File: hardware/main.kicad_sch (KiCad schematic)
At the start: 26 parts, among them J2 Micro_SD_Card, SW1 SW_DIP_x01, SW2 SW_DIP_x01, SW3 SW_DIP_x01, SW4 SW_DIP_x01, SW5 SW_DIP_x01, SW6 SW_DIP_x01, SW7 SW_DIP_x01, U1 SN74LVC245APW, U2 SN74LVC245APW, U3 SN74LVC245APW, U4 Z084000xP

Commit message: update pcb files
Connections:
- net KEYB: now also A1.34 (GPIO28_ADC2); no longer A1.32 (GPIO27_ADC1)
- net IORQ: now reaches U4.20 (~{IORQ})
- net IORQ: now also A1.31 (GPIO26_ADC0)
- net WR: now reaches U4.22 (~{WR})
- net WR: now also A1.32 (GPIO27_ADC1)
- no-connect marks 11 -> 7
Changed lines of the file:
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@@
 		(title "Z80neo")
 		(date "25/10/25")
-		(rev "0.1")
+		(rev "0.2")
 		(company "Jauria Studios")
 	)
@@
 	)
 	(no_connect
-		(at 260.35 127)
-	)
-	(no_connect
-		(at 27.94 81.28)
-	)
-	(no_connect
 		(at 27.94 68.58)
 	)
@@
 	)
 	(no_connect
-		(at 260.35 132.08)
-	)
-	(no_connect
-		(at 27.94 76.2)
-	)
-	(no_connect
 		(at 100.33 165.1)
 	)
@@
 		)
 	)
+	(wire
+		(pts
+			(xy 260.35 129.54) (xy 266.7 129.54)
+		)
+		(stroke
+			(width 0)
+			(type default)
+		)
+	)
 	(bus
 		(pts
@@
 	(wire
 		(pts
-			(xy 260.35 129.54) (xy 266.7 129.54)
+			(xy 260.35 132.08) (xy 266.7 132.08)
 		)
 		(stroke
@@
 	(bus
 		(pts
-			(xy 68.58 99.06) (xy 68.58 101.6)
+			(xy 68.58 100.33) (xy 68.58 101.6)
 		)
 		(stroke
@@
 		)
 	)
+	(wire
+		(pts
+			(xy 27.94 81.28) (xy 21.59 81.28)
+		)
+		(stroke
+			(width 0)
+			(type default)
+		)
+	)
 	(bus
 		(pts
@@
 	(wire
 		(pts
+			(xy 260.35 127) (xy 266.7 127)
+		)
+		(stroke
+			(width 0)
+			(type default)
+		)
+	)
+	(wire
+		(pts
 			(xy 210.82 121.92) (xy 214.63 121.92)
 		)
@@
 	(bus
 		(pts
-			(xy 68.58 99.06) (xy 96.52 99.06)
+			(xy 68.58 100.33) (xy 96.52 100.33)
 		)
 		(stroke
@@
 	(bus
 		(pts
-			(xy 96.52 99.06) (xy 96.52 104.14)
+			(xy 96.52 100.33) (xy 96.52 104.14)
 		)
 		(stroke
@@
 	(wire
 		(pts
+			(xy 27.94 76.2) (xy 21.59 76.2)
+		)
+		(stroke
+			(width 0)
+			(type default)
+		)
+	)
+	(wire
+		(pts
 			(xy 53.34 91.44) (xy 63.5 91.44)
 		)
@@
 		)
 	)
+	(label "B[0..7]"
+		(at 162.56 19.05 0)
+		(effects
+			(font
+				(size 1.27 1.27)
+			)
+			(justify left bottom)
+		)
+	)
 	(label "D0"
 		(at 105.41 106.68 180)
@@
 		)
 	)
+	(label "D[0..7]"
+		(at 74.93 100.33 0)
+		(effects
+			(font
+				(size 1.27 1.27)
+			)
+			(justify left bottom)
+		)
+	)
 	(label "B2"
 		(at 175.26 54.61 0)
@@
 		)
 	)
+	(label "A[0..15]"
+		(at 77.47 22.86 0)
+		(effects
+			(font
+				(size 1.27 1.27)
+			)
+			(justify left bottom)
+		)
+	)
 	(label "D3"
 		(at 105.41 114.3 180)
@@
 		)
 	)
+	(global_label "IORQ"
+		(shape input)
+		(at 21.59 76.2 180)
+		(fields_autoplaced yes)
+		(effects
+			(font
+				(size 1.27 1.27)
+			)
+			(justify right)
+		)
+		(property "Intersheetrefs" "${INTERSHEET_REFS}"
+			(at 14.069 76.2 0)
+			(effects
+				(font
+					(size 1.27 1.27)
+				)
+				(justify right)
+				(hide yes)
+			)
+		)
+	)
 	(global_label "SDA"
 		(shape input)
@@
 		)
 	)
+	(global_label "WR"
+		(shape input)
+		(at 21.59 81.28 180)
+		(fields_autoplaced yes)
+		(effects
+			(font
+				(size 1.27 1.27)
+			)
+			(justify right)
+		)
+		(property "Intersheetrefs" "${INTERSHEET_REFS}"
+			(at 15.8834 81.28 0)
+			(effects
+				(font
+					(size 1.27 1.27)
+				)
+				(justify right)
+				(hide yes)
+			)
+		)
+	)
 	(global_label "SEL2"
 		(shape input)
@@
 		)
 	)
+	(global_label "IORQ"
+		(shape input)
+		(at 266.7 127 0)
+		(fields_autoplaced yes)
+		(effects
+			(font
+				(size 1.27 1.27)
+			)
+			(justify left)
+		)
+		(property "Intersheetrefs" "${INTERSHEET_REFS}"
+			(at 274.221 127 0)
+			(effects
+				(font
+					(size 1.27 1.27)
+				)
+				(justify left)
+				(hide yes)
+			)
+		)
+	)
 	(global_label "RD"
 		(shape input)
@@
 		)
 	)
+	(global_label "WR"
+		(shape input)
+		(at 266.7 129.54 0)
+		(fields_autoplaced yes)
+		(effects
+			(font
+				(size 1.27 1.27)
+			)
+			(justify left)
+		)
+		(property "Intersheetrefs" "${INTERSHEET_REFS}"
+			(at 272.4066 129.54 0)
+			(effects
+				(font
+					(size 1.27 1.27)
+				)
+				(justify left)
+				(hide yes)
+			)
+		)
+	)
 	(global_label "MOSI"
 		(shape input)
@@
 	(global_label "KEYB"
 		(shape input)
-		(at 266.7 129.54 0)
+		(at 266.7 132.08 0)
 		(fields_autoplaced yes)
 		(effects
@@
 		)
 		(property "Intersheetrefs" "${INTERSHEET_REFS}"
-			(at 274.4628 129.54 0)
+			(at 274.4628 132.08 0)
 			(effects
 				(font

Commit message: pcb routing
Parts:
- added R10: R_Small, symbol Device:R_Small
- C1, C2, C3: footprint (none) -> Capacitor_SMD:C_0603_1608Metric_Pad1.08x0.95mm_HandSolder
- D1: footprint (none) -> LED_SMD:LED_0603_1608Metric_Pad1.05x0.95mm_HandSolder
- J2: footprint (none) -> Connector_PinSocket_2.54mm:PinSocket_1x08_P2.54mm_Horizontal
- R1, R2, R3, R4, R5, R6, R7, R8, R9: footprint (none) -> Resistor_SMD:R_0603_1608Metric_Pad0.98x0.95mm_HandSolder
- SW1, SW2, SW3, SW4, SW5, SW6, SW7: footprint (none) -> Button_Switch_THT:SW_PUSH_6mm
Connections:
- net +5V: now also R10.1; no longer D1.2 (A)
- new net: D1.2 (A), R10.2
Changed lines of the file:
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@@
 	(wire
 		(pts
+			(xy 266.7 39.37) (xy 266.7 44.45)
+		)
+		(stroke
+			(width 0)
+			(type default)
+		)
+	)
+	(wire
+		(pts
 			(xy 266.7 58.42) (xy 266.7 60.96)
 		)
@@
 			)
 		)
-		(property "Footprint" ""
+		(property "Footprint" "Resistor_SMD:R_0603_1608Metric_Pad0.98x0.95mm_HandSolder"
 			(at 106.68 97.79 0)
 			(effects
@@
 			)
 		)
-		(property "Footprint" ""
+		(property "Footprint" "Resistor_SMD:R_0603_1608Metric_Pad0.98x0.95mm_HandSolder"
 			(at 171.45 144.78 0)
 			(effects
@@
 			)
 		)
-		(property "Footprint" ""
+		(property "Footprint" "Resistor_SMD:R_0603_1608Metric_Pad0.98x0.95mm_HandSolder"
 			(at 40.64 167.64 0)
 			(effects
@@
 	(symbol
 		(lib_id "power:+5V")
-		(at 266.7 49.53 0)
+		(at 266.7 39.37 0)
 		(unit 1)
 		(exclude_from_sim no)
@@
 		(on_board yes)
 		(dnp no)
-		(fields_autoplaced yes)
 		(property "Reference" "#PWR015"
-			(at 266.7 53.34 0)
+			(at 266.7 43.18 0)
 			(effects
 				(font
@@
 		)
 		(property "Value" "+5V"
-			(at 266.7 44.45 0)
+			(at 266.7 34.29 0)
 			(effects
 				(font
@@
 		)
 		(property "Footprint" ""
-			(at 266.7 49.53 0)
+			(at 266.7 39.37 0)
 			(effects
 				(font
@@
 		)
 		(property "Datasheet" ""
-			(at 266.7 49.53 0)
+			(at 266.7 39.37 0)
 			(effects
 				(font
@@
 		)
 		(property "Description" "Power symbol creates a global label with name \"+5V\""
-			(at 266.7 49.53 0)
+			(at 266.7 39.37 0)
 			(effects
 				(font
@@
 			)
 		)
-		(property "Footprint" ""
+		(property "Footprint" "Capacitor_SMD:C_0603_1608Metric_Pad1.08x0.95mm_HandSolder"
 			(at 240.03 33.02 0)
 			(effects
@@
 			)
 		)
-		(property "Footprint" ""
+		(property "Footprint" "Resistor_SMD:R_0603_1608Metric_Pad0.98x0.95mm_HandSolder"
 			(at 171.45 152.4 0)
 			(effects
@@
 			)
 		)
-		(property "Footprint" ""
+		(property "Footprint" "Button_Switch_THT:SW_PUSH_6mm"
 			(at 162.56 148.59 0)
 			(effects
@@
 			)
 		)
-		(property "Footprint" ""
+		(property "Footprint" "Resistor_SMD:R_0603_1608Metric_Pad0.98x0.95mm_HandSolder"
 			(at 146.05 40.64 0)
 			(effects
@@
 	)
 	(symbol
+		(lib_id "Device:R_Small")
+		(at 266.7 46.99 0)
+		(unit 1)
+		(exclude_from_sim no)
+		(in_bom yes)
+		(on_board yes)
+		(dnp no)
+		(property "Reference" "R10"
+			(at 260.604 47.244 0)
+			(effects
+				(font
+					(size 1.016 1.016)
+				)
+				(justify left)
+			)
+		)
+		(property "Value" "R_Small"
+			(at 269.24 48.2599 0)
+			(effects
+				(font
+					(size 1.27 1.27)
+				)
+				(justify left)
+			)
+		)
+		(property "Footprint" ""
+			(at 266.7 46.99 0)
+			(effects
+				(font
+					(size 1.27 1.27)
+				)
+				(hide yes)
+			)
+		)
+		(property "Datasheet" "~"
+			(at 266.7 46.99 0)
+			(effects
+				(font
+					(size 1.27 1.27)
+				)
+				(hide yes)
+			)
+		)
+		(property "Description" "Resistor, small symbol"
+			(at 266.7 46.99 0)
+			(effects
+				(font
+					(size 1.27 1.27)
+				)
+				(hide yes)
+			)
+		)
+		(pin "2"
+		)
+		(pin "1"
+		)
+		(instances
+			(project ""
+				(path "/7ca8aba6-072c-4d14-9481-2a37d5b8002f"
+					(reference "R10")
+					(unit 1)
+				)
+			)
+		)
+	)
+	(symbol
 		(lib_id "power:+3.3V")
 		(at 278.13 109.22 0)
@@
 			)
 		)
-		(property "Footprint" ""
+		(property "Footprint" "Resistor_SMD:R_0603_1608Metric_Pad0.98x0.95mm_HandSolder"
 			(at 171.45 137.16 0)
 			(effects
@@
 			)
 		)
-		(property "Footprint" ""
+		(property "Footprint" "Button_Switch_THT:SW_PUSH_6mm"
 			(at 162.56 140.97 0)
 			(effects
@@
 			)
 		)
-		(property "Footprint" ""
+		(property "Footprint" "Resistor_SMD:R_0603_1608Metric_Pad0.98x0.95mm_HandSolder"
 			(at 171.45 160.02 0)
 			(effects
@@
 			)
 		)
-		(property "Footprint" ""
+		(property "Footprint" "Button_Switch_THT:SW_PUSH_6mm"
 			(at 62.23 175.26 0)
 			(effects
@@
 			)
 		)
-		(property "Footprint" ""
+		(property "Footprint" "Connector_PinSocket_2.54mm:PinSocket_1x08_P2.54mm_Horizontal"
 			(at 152.4 165.1 0)
 			(effects
@@
 			)
 		)
-		(property "Footprint" ""
+		(property "Footprint" "Resistor_SMD:R_0603_1608Metric_Pad0.98x0.95mm_HandSolder"
 			(at 171.45 129.54 0)
 			(effects
@@
 			)
 		)
-		(property "Footprint" ""
+		(property "Footprint" "Button_Switch_THT:SW_PUSH_6mm"
 			(at 162.56 133.35 0)
 			(effects
@@
 			)
 		)
-		(property "Footprint" ""
+		(property "Footprint" "Button_Switch_THT:SW_PUSH_6mm"
 			(at 162.56 156.21 0)
 			(effects
@@
 			)
 		)
-		(property "Footprint" ""
+		(property "Footprint" "LED_SMD:LED_0603_1608Metric_Pad1.05x0.95mm_HandSolder"
 			(at 266.7 55.88 90)
 			(effects
@@
 			)
 		)
-		(property "Footprint" ""
+		(property "Footprint" "Capacitor_SMD:C_0603_1608Metric_Pad1.08x0.95mm_HandSolder"
 			(at 224.79 33.02 0)
 			(effects
@@
 			)
 		)
-		(property "Footprint" ""
+		(property "Footprint" "Button_Switch_THT:SW_PUSH_6mm"
 			(at 180.34 109.22 0)
 			(effects
@@
 			)
 		)
-		(property "Footprint" ""
+		(property "Footprint" "Capacitor_SMD:C_0603_1608Metric_Pad1.08x0.95mm_HandSolder"
 			(at 232.41 33.02 0)
 			(effects
@@
 			)
 		)
-		(property "Footprint" ""
+		(property "Footprint" "Button_Switch_THT:SW_PUSH_6mm"
 			(at 162.56 163.83 0)
 			(effects
@@
 			)
 		)
-		(property "Footprint" ""
+		(property "Footprint" "Resistor_SMD:R_0603_1608Metric_Pad0.98x0.95mm_HandSolder"
 			(at 86.36 40.64 0)
 			(effects

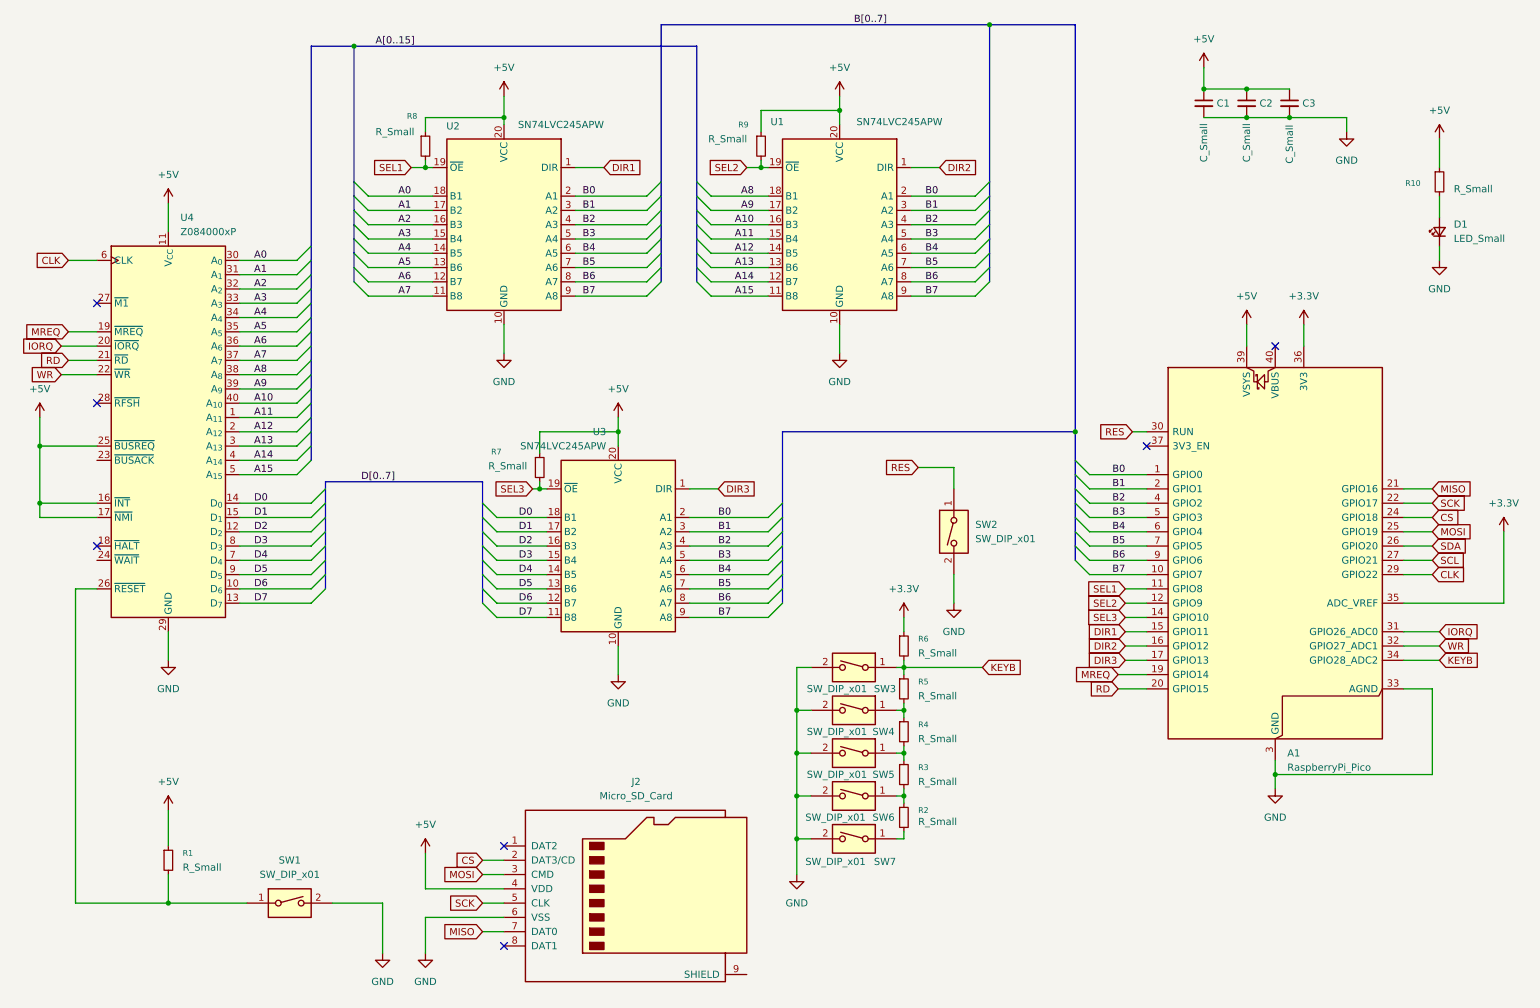
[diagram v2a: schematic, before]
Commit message: disable overclock, back to 150Mhz and add i2c display to schematic
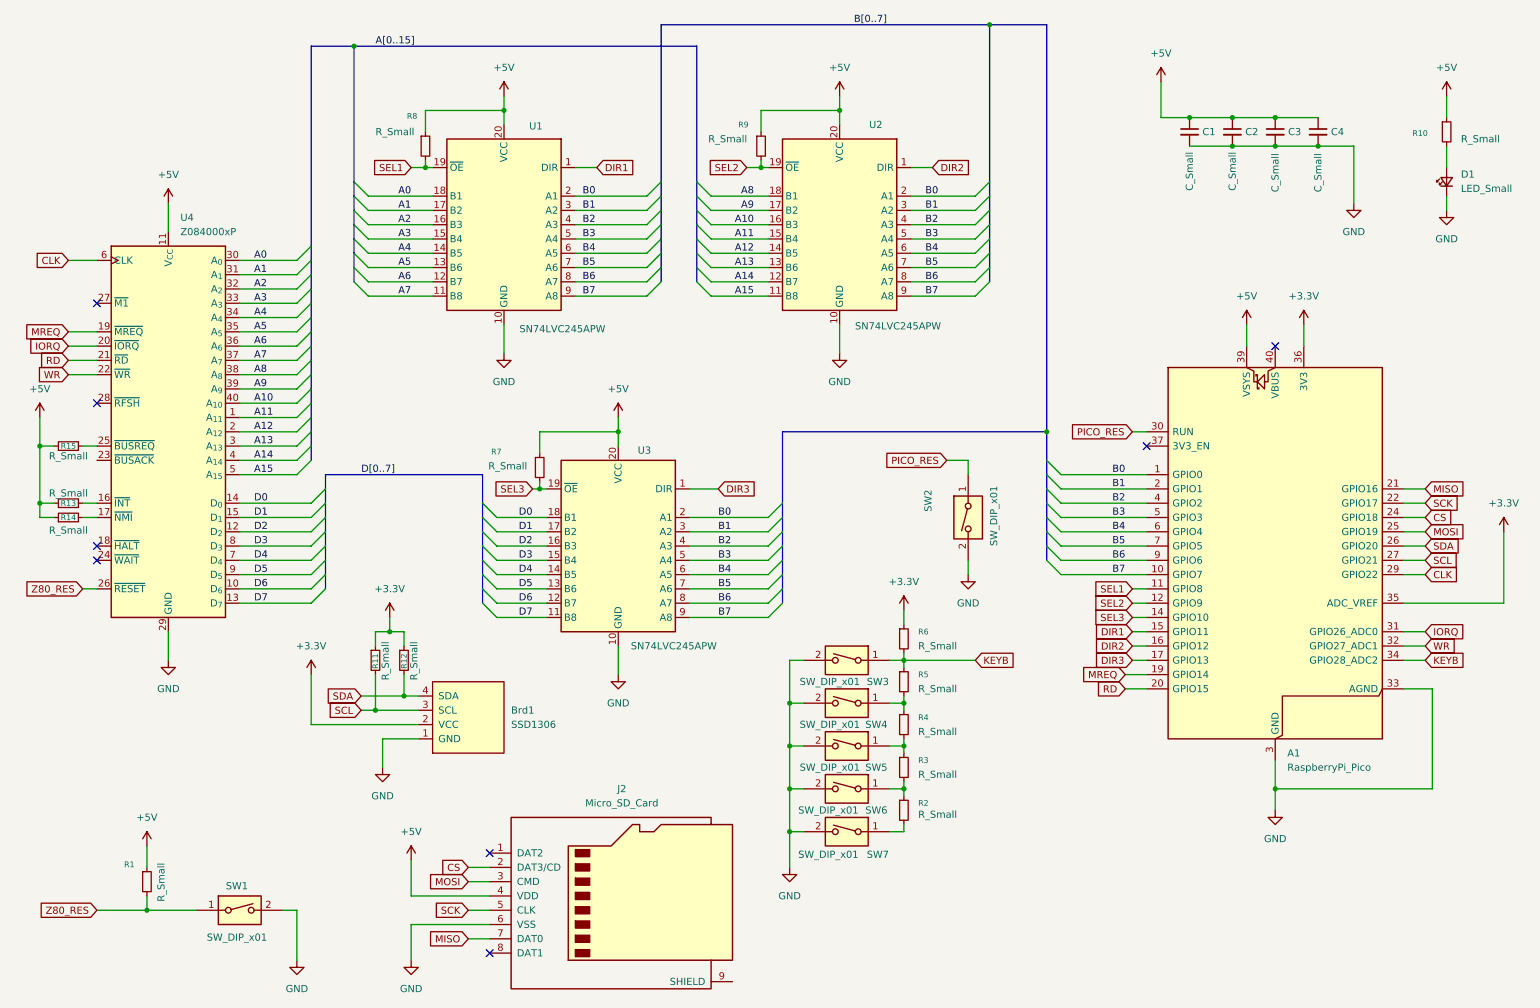
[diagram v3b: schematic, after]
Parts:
- added Brd1: SSD1306, Display:Adafruit_SSD1306_No_Mounting_Holes, symbol SSD1306-128x64_OLED:SSD1306
- added C4: C_Small, Capacitor_SMD:C_0603_1608Metric_Pad1.08x0.95mm_HandSolder, symbol Device:C_Small
- added R11, R12, R13, R14, R15: R_Small, Resistor_SMD:R_0603_1608Metric_Pad0.98x0.95mm_HandSolder, symbol Device:R_Small
- R10: footprint (none) -> Resistor_SMD:R_0603_1608Metric_Pad0.98x0.95mm_HandSolder
- renumbered U2 to U1, U1 to U2
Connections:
- net +3.3V: now also Brd1.2 (VCC), R11.1, R12.1
- net +5V: now also C4.1, R13.1, R14.1, R15.1; no longer U4.16 (~{INT}), U4.17 (~{NMI}), U4.25 (~{BUSREQ})
- net GND: now also Brd1.1 (GND), C4.2
- net SCL: now also Brd1.3 (SCL), R11.2
- net SDA: now also Brd1.4 (SDA), R12.2
- net Z80_RES: now reaches R1.2, SW1.1, U4.26 (~{RESET})
- net RES renamed PICO_RES
- new net: R15.2, U4.25 (~{BUSREQ})
- new net: R13.2, U4.16 (~{INT})
- new net: R14.2, U4.17 (~{NMI})
- no-connect marks 7 -> 8
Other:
- moved on the sheet: C1, C2, C3, D1, J2, R1, R10, R2, R3, R4, R5, R6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

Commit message: use tht components
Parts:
- C1, C2, C3, C4: footprint Capacitor_SMD:C_0603_1608Metric_Pad1.08x0.95mm_HandSolder -> Capacitor_THT:C_Disc_D4.3mm_W1.9mm_P5.00mm
- D1: footprint LED_SMD:LED_0603_1608Metric_Pad1.05x0.95mm_HandSolder -> LED_THT:LED_D3.0mm
- R1, R10, R11, R12, R13, R14, R15, R2, R3, R4, R5, R6, R7, R8, R9: footprint Resistor_SMD:R_0603_1608Metric_Pad0.98x0.95mm_HandSolder -> Resistor_THT:R_Axial_DIN0207_L6.3mm_D2.5mm_P7.62mm_Horizontal
- U1, U2, U3: footprint Package_SO:TSSOP-20_4.4x6.5mm_P0.65mm -> Package_DIP:CERDIP-20_W7.62mm_SideBrazed_LongPads_Socket
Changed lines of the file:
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@@
 			)
 		)
-		(property "Footprint" "Resistor_SMD:R_0603_1608Metric_Pad0.98x0.95mm_HandSolder"
+		(property "Footprint" "Resistor_THT:R_Axial_DIN0207_L6.3mm_D2.5mm_P7.62mm_Horizontal"
 			(at 106.68 97.79 0)
 			(effects
@@
 			)
 		)
-		(property "Footprint" "Resistor_SMD:R_0603_1608Metric_Pad0.98x0.95mm_HandSolder"
+		(property "Footprint" "Resistor_THT:R_Axial_DIN0207_L6.3mm_D2.5mm_P7.62mm_Horizontal"
 			(at 171.45 143.51 0)
 			(effects
@@
 			)
 		)
-		(property "Footprint" "Resistor_SMD:R_0603_1608Metric_Pad0.98x0.95mm_HandSolder"
+		(property "Footprint" "Resistor_THT:R_Axial_DIN0207_L6.3mm_D2.5mm_P7.62mm_Horizontal"
 			(at 36.83 171.45 0)
 			(effects
@@
 			)
 		)
-		(property "Footprint" "Capacitor_SMD:C_0603_1608Metric_Pad1.08x0.95mm_HandSolder"
+		(property "Footprint" "Capacitor_THT:C_Disc_D4.3mm_W1.9mm_P5.00mm"
 			(at 237.49 38.1 0)
 			(effects
@@
 			)
 		)
-		(property "Footprint" "Resistor_SMD:R_0603_1608Metric_Pad0.98x0.95mm_HandSolder"
+		(property "Footprint" "Resistor_THT:R_Axial_DIN0207_L6.3mm_D2.5mm_P7.62mm_Horizontal"
 			(at 171.45 151.13 0)
 			(effects
@@
 			)
 		)
-		(property "Footprint" "Package_SO:TSSOP-20_4.4x6.5mm_P0.65mm"
+		(property "Footprint" "Package_DIP:CERDIP-20_W7.62mm_SideBrazed_LongPads_Socket"
 			(at 97.79 128.27 0)
 			(effects
@@
 			)
 		)
-		(property "Footprint" "Resistor_SMD:R_0603_1608Metric_Pad0.98x0.95mm_HandSolder"
+		(property "Footprint" "Resistor_THT:R_Axial_DIN0207_L6.3mm_D2.5mm_P7.62mm_Horizontal"
 			(at 146.05 40.64 0)
 			(effects
@@
 			)
 		)
-		(property "Footprint" "Resistor_SMD:R_0603_1608Metric_Pad0.98x0.95mm_HandSolder"
+		(property "Footprint" "Resistor_THT:R_Axial_DIN0207_L6.3mm_D2.5mm_P7.62mm_Horizontal"
 			(at 267.97 38.1 0)
 			(effects
@@
 			)
 		)
-		(property "Footprint" "Resistor_SMD:R_0603_1608Metric_Pad0.98x0.95mm_HandSolder"
+		(property "Footprint" "Resistor_THT:R_Axial_DIN0207_L6.3mm_D2.5mm_P7.62mm_Horizontal"
 			(at 22.86 93.98 0)
 			(effects
@@
 			)
 		)
-		(property "Footprint" "Resistor_SMD:R_0603_1608Metric_Pad0.98x0.95mm_HandSolder"
+		(property "Footprint" "Resistor_THT:R_Axial_DIN0207_L6.3mm_D2.5mm_P7.62mm_Horizontal"
 			(at 171.45 135.89 0)
 			(effects
@@
 			)
 		)
-		(property "Footprint" "Package_SO:TSSOP-20_4.4x6.5mm_P0.65mm"
+		(property "Footprint" "Package_DIP:CERDIP-20_W7.62mm_SideBrazed_LongPads_Socket"
 			(at 137.16 71.12 0)
 			(effects
@@
 			)
 		)
-		(property "Footprint" "Resistor_SMD:R_0603_1608Metric_Pad0.98x0.95mm_HandSolder"
+		(property "Footprint" "Resistor_THT:R_Axial_DIN0207_L6.3mm_D2.5mm_P7.62mm_Horizontal"
 			(at 22.86 104.14 0)
 			(effects
@@
 			)
 		)
-		(property "Footprint" "Resistor_SMD:R_0603_1608Metric_Pad0.98x0.95mm_HandSolder"
+		(property "Footprint" "Resistor_THT:R_Axial_DIN0207_L6.3mm_D2.5mm_P7.62mm_Horizontal"
 			(at 22.86 106.68 0)
 			(effects
@@
 			)
 		)
-		(property "Footprint" "Resistor_SMD:R_0603_1608Metric_Pad0.98x0.95mm_HandSolder"
+		(property "Footprint" "Resistor_THT:R_Axial_DIN0207_L6.3mm_D2.5mm_P7.62mm_Horizontal"
 			(at 171.45 158.75 0)
 			(effects
@@
 			)
 		)
-		(property "Footprint" "Resistor_SMD:R_0603_1608Metric_Pad0.98x0.95mm_HandSolder"
+		(property "Footprint" "Resistor_THT:R_Axial_DIN0207_L6.3mm_D2.5mm_P7.62mm_Horizontal"
 			(at 171.45 128.27 0)
 			(effects
@@
 			)
 		)
-		(property "Footprint" "Resistor_SMD:R_0603_1608Metric_Pad0.98x0.95mm_HandSolder"
+		(property "Footprint" "Resistor_THT:R_Axial_DIN0207_L6.3mm_D2.5mm_P7.62mm_Horizontal"
 			(at 77.47 132.08 0)
 			(effects
@@
 			)
 		)
-		(property "Footprint" "LED_SMD:LED_0603_1608Metric_Pad1.05x0.95mm_HandSolder"
+		(property "Footprint" "LED_THT:LED_D3.0mm"
 			(at 267.97 46.99 90)
 			(effects
@@
 			)
 		)
-		(property "Footprint" "Resistor_SMD:R_0603_1608Metric_Pad0.98x0.95mm_HandSolder"
+		(property "Footprint" "Resistor_THT:R_Axial_DIN0207_L6.3mm_D2.5mm_P7.62mm_Horizontal"
 			(at 82.55 132.08 0)
 			(effects
@@
 			)
 		)
-		(property "Footprint" "Capacitor_SMD:C_0603_1608Metric_Pad1.08x0.95mm_HandSolder"
+		(property "Footprint" "Capacitor_THT:C_Disc_D4.3mm_W1.9mm_P5.00mm"
 			(at 222.25 38.1 0)
 			(effects
@@
 			)
 		)
-		(property "Footprint" "Capacitor_SMD:C_0603_1608Metric_Pad1.08x0.95mm_HandSolder"
+		(property "Footprint" "Capacitor_THT:C_Disc_D4.3mm_W1.9mm_P5.00mm"
 			(at 229.87 38.1 0)
 			(effects
@@
 			)
 		)
-		(property "Footprint" "Capacitor_SMD:C_0603_1608Metric_Pad1.08x0.95mm_HandSolder"
+		(property "Footprint" "Capacitor_THT:C_Disc_D4.3mm_W1.9mm_P5.00mm"
 			(at 245.11 38.1 0)
 			(effects
@@
 			)
 		)
-		(property "Footprint" "Package_SO:TSSOP-20_4.4x6.5mm_P0.65mm"
+		(property "Footprint" "Package_DIP:CERDIP-20_W7.62mm_SideBrazed_LongPads_Socket"
 			(at 77.47 71.12 0)
 			(effects
@@
 			)
 		)
-		(property "Footprint" "Resistor_SMD:R_0603_1608Metric_Pad0.98x0.95mm_HandSolder"
+		(property "Footprint" "Resistor_THT:R_Axial_DIN0207_L6.3mm_D2.5mm_P7.62mm_Horizontal"
 			(at 86.36 40.64 0)
 			(effects
